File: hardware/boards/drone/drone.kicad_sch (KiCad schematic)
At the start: 76 parts, among them J1 SMA, J2 2-pin 1.27mm, Q1 2N7000, U1 SX1262IMLTRT, U2 SKY13453-385LF, U3 LSM6DSM, U4 RP2040, U5 IS31FL3197, U6 L80-R, Y1 32 MHz, Y2 32 MHz

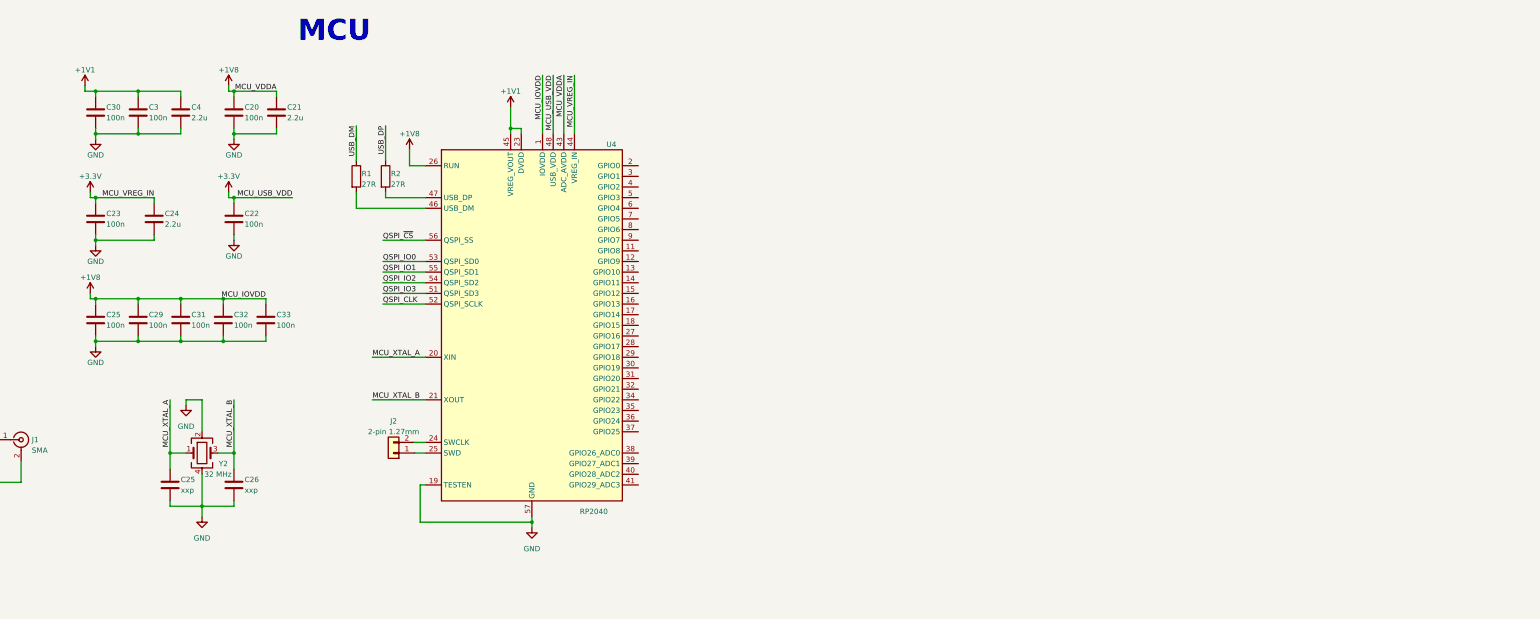
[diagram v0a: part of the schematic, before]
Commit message: Add MCU flash and USB-PD
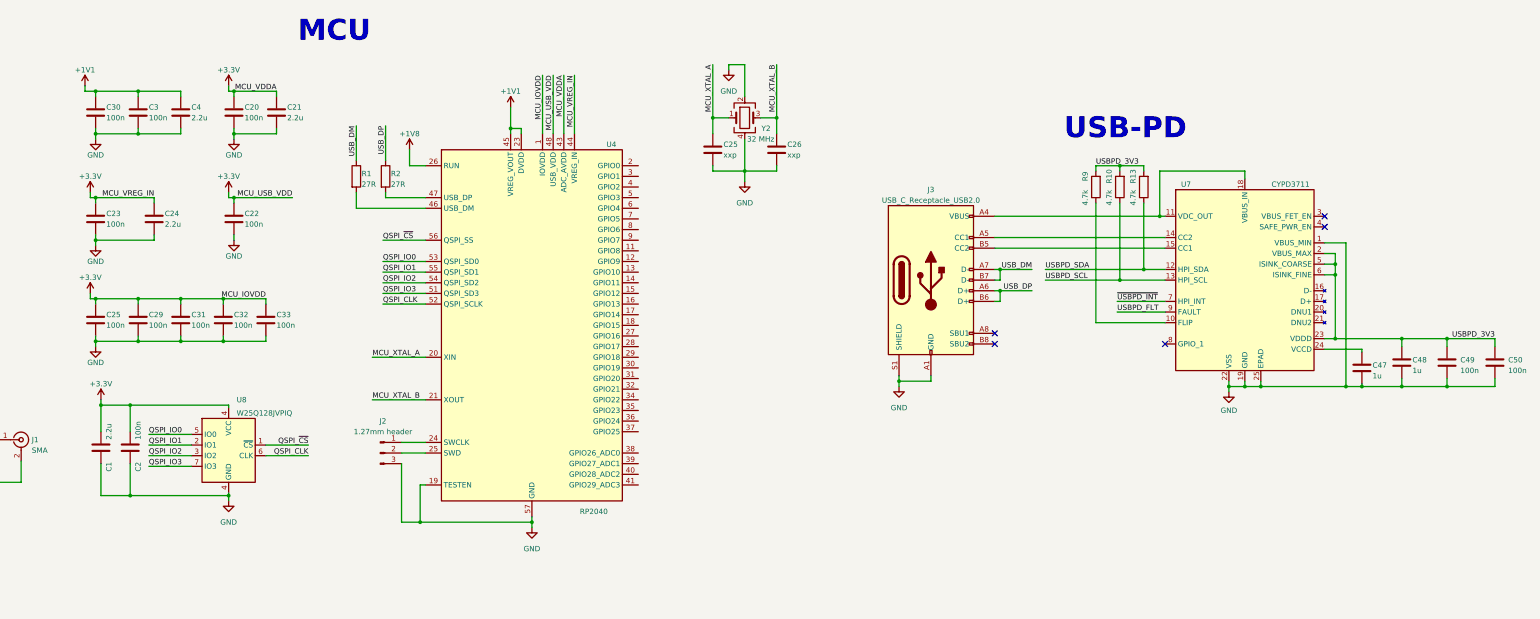
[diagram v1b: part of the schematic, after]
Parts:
- removed J2: 2-pin 1.27mm, symbol Connector_Generic:Conn_01x02
- added C1: 2.2u, Capacitor_SMD:C_0201_0603Metric, symbol Device:C
- added C2: 100n, Capacitor_SMD:C_0201_0603Metric, symbol Device:C
- added C47, C48: 1u, symbol Device:C
- added C49, C50: 100n, symbol Device:C
- added J2: 1.27mm header, symbol Connector:Conn_01x03_Pin
- added J3: USB_C_Receptacle_USB2.0, symbol Connector:USB_C_Receptacle_USB2.0
- added R10, R13, R9: 4.7k, symbol Device:R
- added U7: CYPD3711, Package_DFN_QFN:QFN-24-1EP_4x4mm_P0.5mm_EP2.7x2.7mm, symbol Capstone:CYPD3711-24LQXQ
- added U8: W25Q128JVPIQ, symbol Memory_Flash:W25Q128JVPIQ
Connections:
- net +1V8: no longer C20.1, C21.1, C25.1, C29.1, C31.1, C32.1, C33.1, U4.1 (IOVDD), U4.10 (IOVDD), U4.22 (IOVDD), U4.33 (IOVDD), U4.42 (IOVDD), U4.43 (ADC_AVDD), U4.49 (IOVDD)
- net +3.3V: now also C20.1, C21.1, C25.1, C29.1, C31.1, C32.1, C33.1, U4.1 (IOVDD), U4.10 (IOVDD), U4.22 (IOVDD), U4.33 (IOVDD), U4.42 (IOVDD), U4.43 (ADC_AVDD), U4.49 (IOVDD), C1.1, C2.1, U8.4 (VCC)
- net GND: now also C1.2, C2.2, C47.2, C48.2, C49.2, C50.2, J2.3 (Pin_3), J3.A1 (GND), J3.A12 (GND), J3.B1 (GND), J3.B12 (GND), J3.S1 (SHIELD), U7.1 (VBUS_MIN), U7.19 (GND), U7.22 (VSS), U7.25 (EPAD), U8.4 (VCC)
- net QSPI_CLK: now also U8.6 (CLK)
- net QSPI_IO0: now also U8.5 (IO0)
- net QSPI_IO1: now also U8.2 (IO1)
- net QSPI_IO2: now also U8.3 (IO2)
- net QSPI_IO3: now also U8.7 (IO3)
- net QSPI_~{CS}: now also U8.1 (~{CS})
- net USB_DM: now also J3.A7 (D-), J3.B7 (D-)
- net USB_DP: now also J3.A6 (D+), J3.B6 (D+)
- net at U4.24 (SWCLK): now also J2.1 (Pin_1)
- net at U4.25 (SWD): now also J2.2 (Pin_2)
- new net: R9.1, U7.10 (FLIP)
- new net: J3.A4 (VBUS), J3.A9 (VBUS), J3.B4 (VBUS), J3.B9 (VBUS), U7.11 (VDC_OUT), U7.18 (VBUS_IN)
- new net: J3.A5 (CC1), U7.14 (CC2)
- new net: J3.B5 (CC2), U7.15 (CC1)
- new net: C47.1, U7.24 (VCCD)
- new net USBPD_3V3: C48.1, C49.1, C50.1, R10.2, R13.2, R9.2, U7.2 (VBUS_MAX), U7.23 (VDDD), U7.5 (ISINK_COARSE), U7.6 (ISINK_FINE)
- new net USBPD_FLT: U7.9 (FAULT)
- new net USBPD_SCL: R10.1, U7.13 (HPI_SCL)
- new net USBPD_SDA: R13.1, U7.12 (HPI_SDA)
- new net ~{USBPD_INT}: U7.7 (HPI_INT)
- no-connect marks 6 -> 11
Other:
- note added: "USB-PD"
- moved on the sheet: C25, C26, Y2

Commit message: Add Shane + Dylan's first draft schematics
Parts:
- removed BZ1: Buzzer, symbol Device:Buzzer
- removed C1: 2.2u, Capacitor_SMD:C_0201_0603Metric, symbol Device:C
- removed C1, C2, C25, C26: xxp, symbol Device:C
- removed C10, C20, C21, C22: 1n, symbol Device:C
- removed C11, C13: 5.6p, symbol Device:C
- removed C12: 3p, symbol Device:C
- removed C14, C19: 39p, symbol Device:C
- removed C15, C7: 1.8p, symbol Device:C
- removed C16, C23, C24, C3, C43, C45, C46, C49, C50: 100n, symbol Device:C
- removed C17, C18: 3.3p, symbol Device:C
- removed C2, C20, C22, C23, C25, C29, C3, C30, C31, C32, C33: 100n, Capacitor_SMD:C_0201_0603Metric, symbol Device:C
- removed C21, C24, C4: 2.2u, Capacitor_SMD:C_0402_1005Metric, symbol Device:C
- removed C4, C40, C41, C47, C48: 1u, symbol Device:C
- removed C42, C44: 2.2u, symbol Device:C
- removed C5: 47n, symbol Device:C
- removed C6: 47p, symbol Device:C
- removed C8: 470n, symbol Device:C
- removed C9: 2.4p, symbol Device:C
- removed D1: TC5050RGBW, symbol Capstone:TC5050RGBW
- removed J1: SMA, symbol Connector:Conn_Coaxial
- removed J2: 1.27mm header, symbol Connector:Conn_01x03_Pin
- removed J3: USB_C_Receptacle_USB2.0, symbol Connector:USB_C_Receptacle_USB2.0
- removed L1: 47n, symbol Device:L
- removed L2: 0R, symbol Device:L
- removed L3: 15n, symbol Device:L
- removed L4: 15u, symbol Device:L
- removed L5: 2.5n, symbol Device:L
- removed L6: 4.7n, symbol Device:L
- removed L7: 9.1n, symbol Device:L
- removed Q1: 2N7000, Package_TO_SOT_THT:TO-92_Inline, symbol Transistor_FET:2N7000
- removed R1: 100R, symbol Device:R
- removed R1, R2: 27R, Resistor_SMD:R_0201_0603Metric, symbol Device:R
- removed R10, R13, R2, R3, R9: 4.7k, symbol Device:R
- removed R4: 7.5k, symbol Device:R
- removed R5: 100k, symbol Device:R
- removed R6, R7: 1k, symbol Device:R
- removed R8: 330R, symbol Device:R
- removed U1: SX1262IMLTRT, QFN50P400X400X100-25N, symbol Capstone:SX1262IMLTRT
- removed U2: SKY13453-385LF, IC_SKY13453-385LF, symbol Capstone:SKY13453-385LF
- removed U3: LSM6DSM, Package_LGA:LGA-14_3x2.5mm_P0.5mm_LayoutBorder3x4y, symbol Capstone:LSM6DSM
- removed U4: RP2040, Package_DFN_QFN:QFN-56-1EP_7x7mm_P0.4mm_EP3.2x3.2mm, symbol MCU_RaspberryPi:RP2040
- removed U5: IS31FL3197, Package_DFN_QFN:QFN-16-1EP_4x4mm_P0.65mm_EP2.1x2.1mm, symbol Capstone:IS31FL3197
- removed U6: L80-R, RF_GPS:Quectel_L80-R, symbol RF_GPS:L80-R
- removed U7: CYPD3711, Package_DFN_QFN:QFN-24-1EP_4x4mm_P0.5mm_EP2.7x2.7mm, symbol Capstone:CYPD3711-24LQXQ
- removed U8: W25Q128JVPIQ, symbol Memory_Flash:W25Q128JVPIQ
- removed Y1, Y2: 32 MHz, symbol Device:Crystal_GND24
- added C69: 100n, symbol Device:C
- added R30, R31, R32, R33: 10k, Resistor_SMD_AKL:R_MELF_MMB-0207, symbol Device:R
- added U18: TCA9539RTWR, symbol Capstone:TCA9539RTWR_
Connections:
- net GND: now also C69.2, U18.23 (A1), U18.9 (GND)
- new net +3V3: C69.1, R30.1, R31.1, R32.1, R33.1, U18.18 (A0), U18.21 (VCC)
- new net PWR_IOX_SCL: R30.2, U18.19 (SCL)
- new net PWR_IOX_SDA: R31.2, U18.20 (SDA)
- new net ~{PWR_IOX_INT}: R33.2, U18.22 (~{INT})
- new net ~{PWR_IOX_RST}: R32.2, U18.24 (~{RESET})
- no-connect marks 11 -> 0
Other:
- added sheet Digital Radio (digital_radio.kicad_sch)
- added sheet GPS (gps.kicad_sch)
- added sheet IMU (imu.kicad_sch)
- added sheet Indication (indication.kicad_sch)
- added sheet LV Power (lv_pwr.kicad_sch)
- added sheet MCU (mcu.kicad_sch)
- added sheet MCU IO (mcu_io.kicad_sch)
- added sheet Motors (motors.kicad_sch)
- added sheet USB and USB-PD (usb.kicad_sch)
- added sheet Video Radio (video_radio.kicad_sch)
- note added: "ALL THE UNCONNECTED PINS HERE ARE FOR STEFAN'S STUFF"
- note added: "I2C ADDRESS: 0x75"
- note added: "I2C0: MOTORS, MISC I2C1: POWER"
- note added: "STEFAN'S IO EXPANDER LOL"
- note removed: "BUZZER"
- note removed: "DIGITAL RADIO"
- note removed: "GPS"
- note removed: "IMU"
- note removed: "LED"
- note removed: "MCU"
- note removed: "USB-PD"

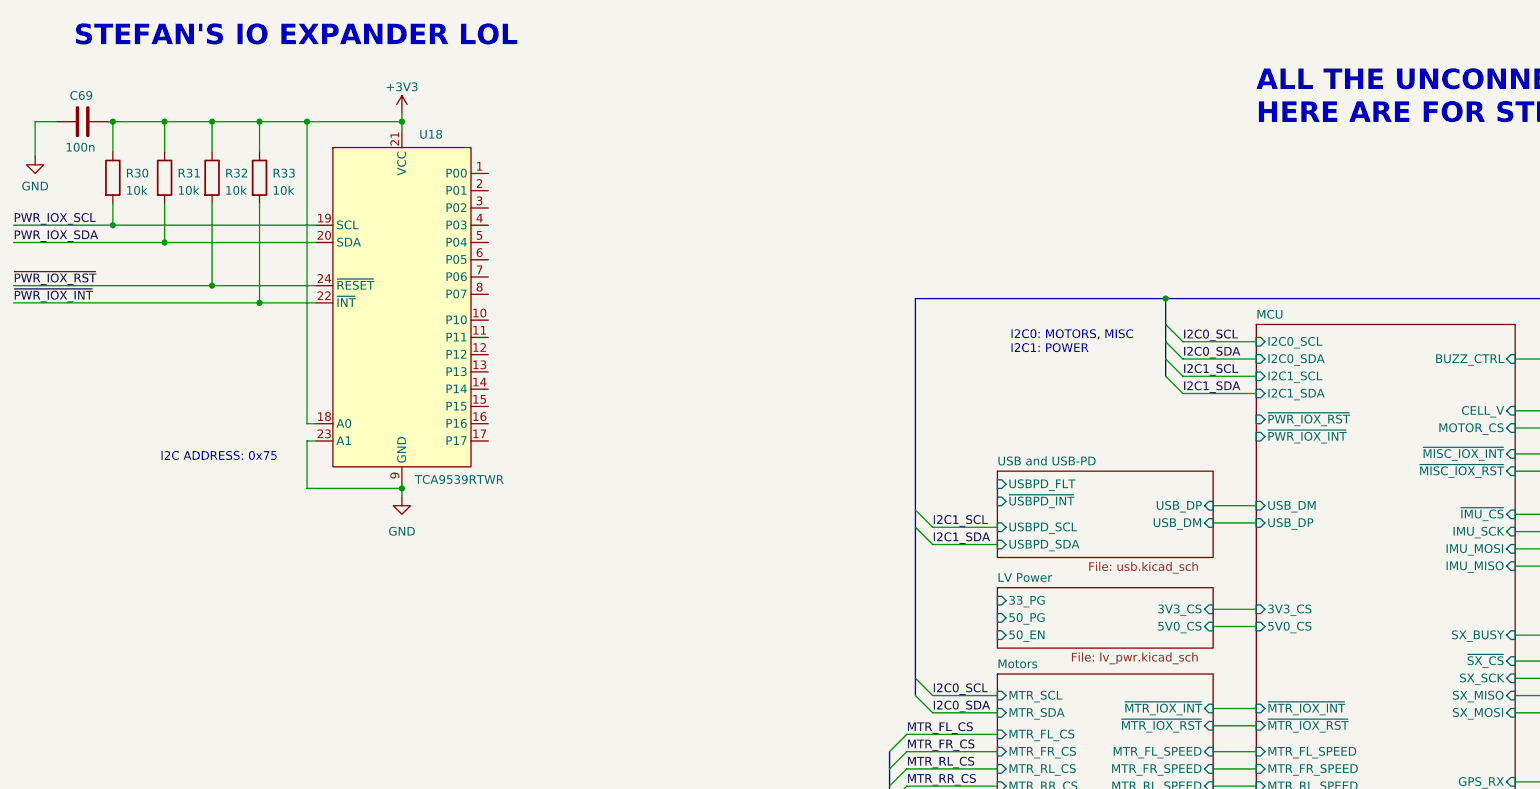
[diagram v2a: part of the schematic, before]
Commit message: Added Power & Charging Subsystems
- Replaced Qi receiver
- Added charge controller
- Added BMS
- Added switch between Qi & USB-PD
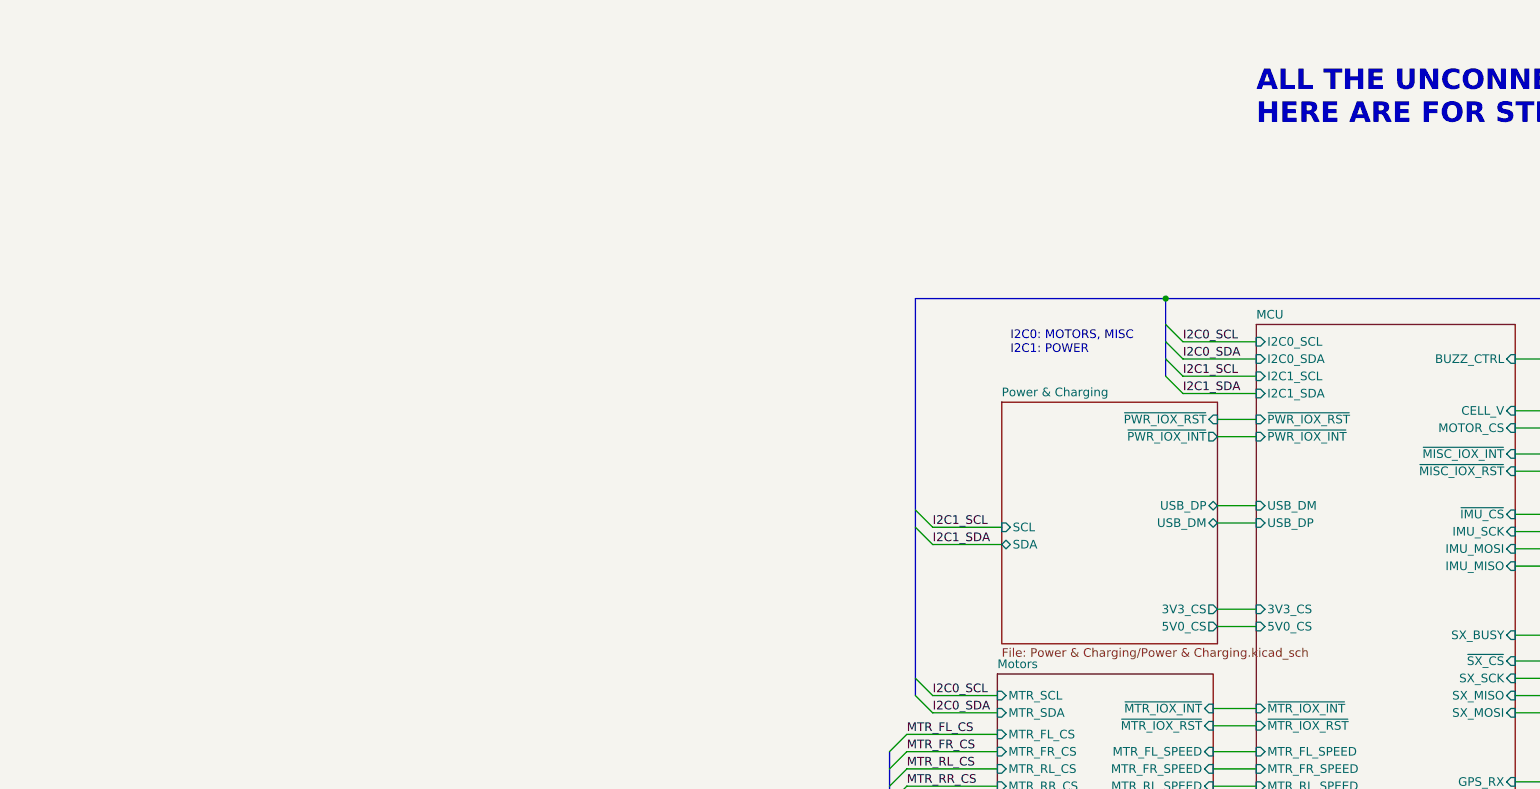
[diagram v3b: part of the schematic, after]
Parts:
- removed C69: 100n, symbol Device:C
- removed R30, R31, R32, R33: 10k, Resistor_SMD_AKL:R_MELF_MMB-0207, symbol Device:R
- removed U18: TCA9539RTWR, symbol Capstone:TCA9539RTWR_
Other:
- removed sheet LV Power
- removed sheet USB and USB-PD
- added sheet Power & Charging (Power & Charging/Power & Charging.kicad_sch)
- note removed: "I2C ADDRESS: 0x75"
- note removed: "STEFAN'S IO EXPANDER LOL"
